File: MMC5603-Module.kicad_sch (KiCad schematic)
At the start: 16 parts, among them CN1 AFC10-S04QCA-00, J1 Conn_01x04_Pin, Q1 2N7002KDW, U1 MMC5633NJ, U2 MIC5504-1.8YM5

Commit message: update license
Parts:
- U1: value MMC5633NJ -> MMC5603NJ
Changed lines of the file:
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@@
       (effects (font (size 1.27 1.27)) (justify left))
     )
-    (property "Value" "MMC5633NJ" (at 90.17 109.855 0)
+    (property "Value" "MMC5603NJ" (at 90.17 109.855 0)
       (effects (font (size 1.27 1.27)) (justify left))
     )

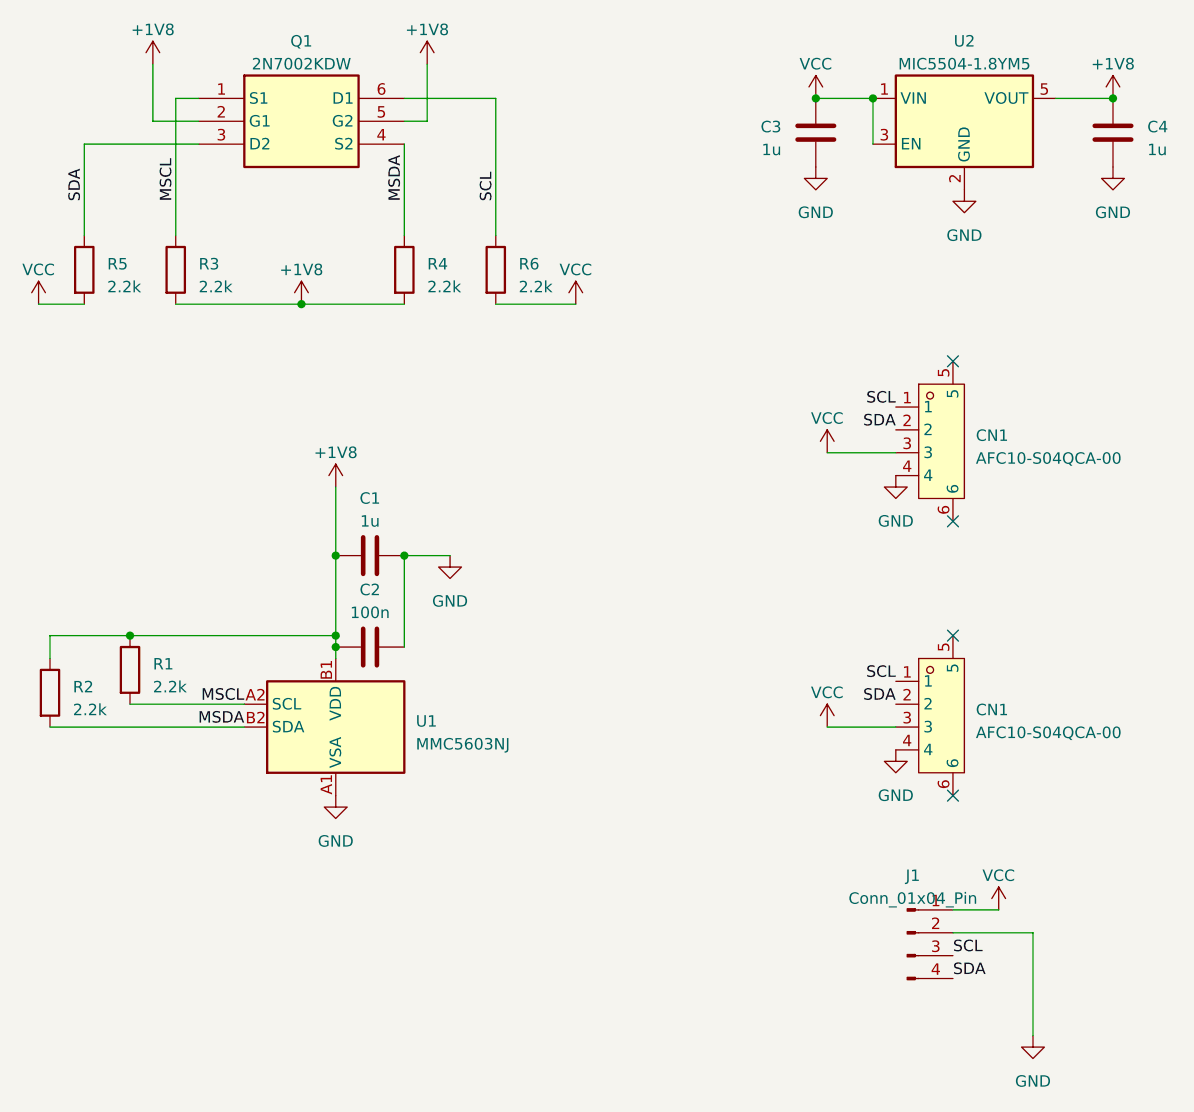
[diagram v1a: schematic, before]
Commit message: ditch logic shift, fix qwiic pinout, documentation
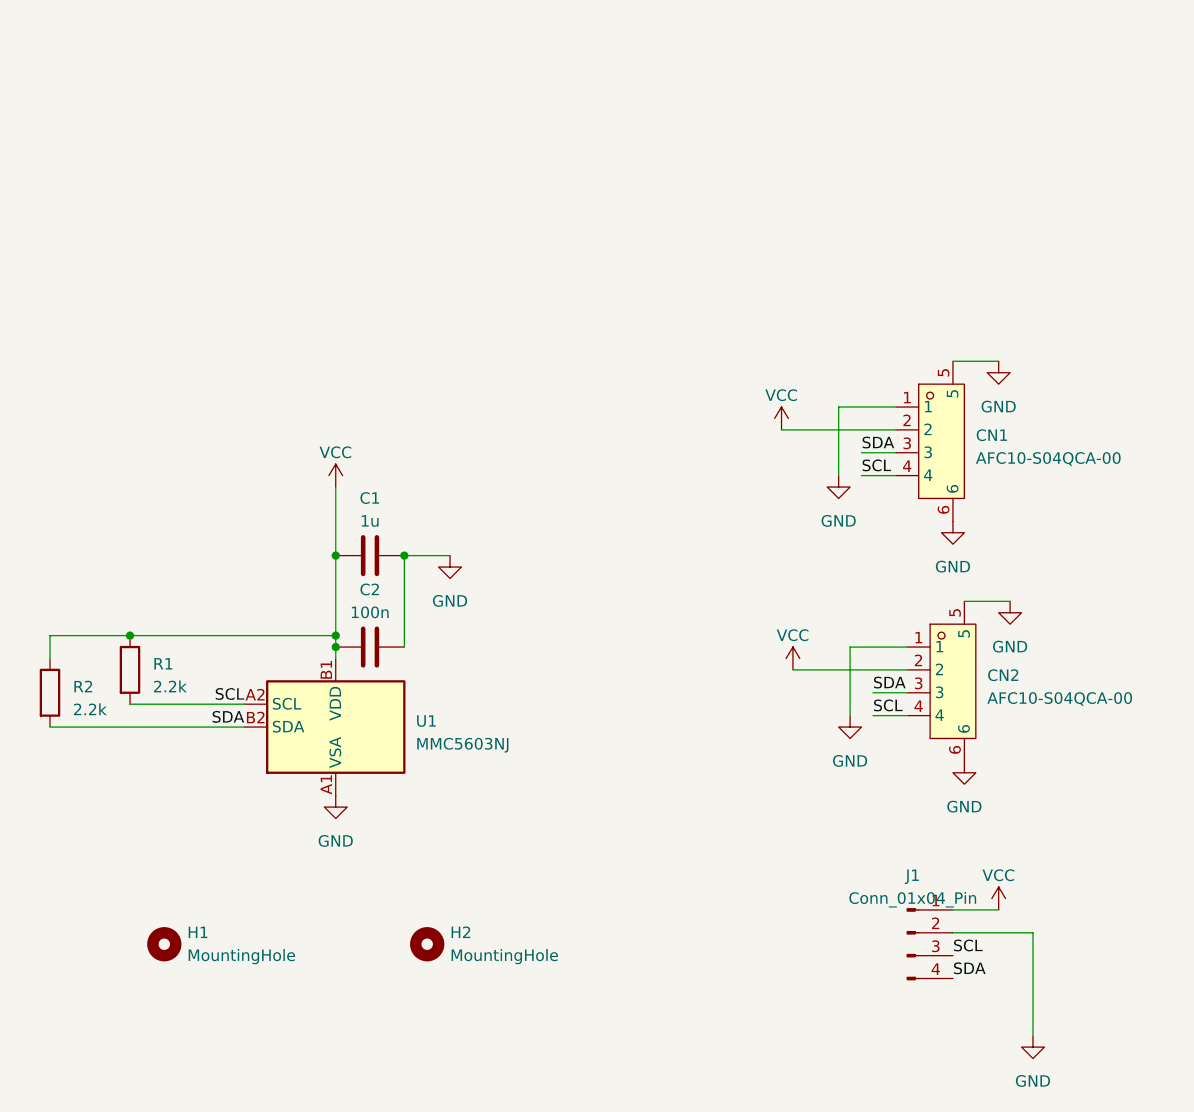
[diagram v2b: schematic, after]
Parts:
- removed C3, C4: 1u, Capacitor_SMD:C_0603_1608Metric, symbol Device:C
- removed CN1: AFC10-S04QCA-00, MMC5603-Module:CONN-SMD_AFC10-S04QCA-00, symbol BMI270-Breakout:AFC10-S04QCA-00
- removed Q1: 2N7002KDW, 2n7002:SOT65P210X110-6N, symbol 2n7002:2N7002KDW_R1_00001
- removed R3, R4, R5, R6: 2.2k, Resistor_SMD:R_0402_1005Metric, symbol Device:R
- removed U2: MIC5504-1.8YM5, Package_TO_SOT_SMD:SOT-23-5, symbol Regulator_Linear:MIC5504-1.8YM5
- added CN2: AFC10-S04QCA-00, MMC5603-Module:CONN-SMD_AFC10-S04QCA-00, symbol BMI270-Breakout:AFC10-S04QCA-00
- added H1, H2: MountingHole, MountingHole:MountingHole_2.2mm_M2, symbol Mechanical:MountingHole
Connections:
- net +1V8 is gone; now on net VCC: C1.1, C2.1, R1.1, R2.1, U1.B1 (VDD)
- net MSCL is gone; now on net SCL: R1.2, U1.A2 (SCL)
- net MSDA is gone; now on net SDA: R2.2, U1.B2 (SDA)
- net GND: now also CN1.1, CN1.5, CN1.6, CN2.1, CN2.5, CN2.6; no longer CN1.4
- net SCL: now also CN1.4, CN2.4; no longer CN1.1
- net SDA: now also CN1.3, CN2.3; no longer CN1.2
- net VCC: now also CN1.2, CN2.2; no longer CN1.3
- no-connect marks 4 -> 0
